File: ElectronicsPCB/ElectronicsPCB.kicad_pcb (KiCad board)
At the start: 4 copper layers, 67.8 x 80.8 mm, 44 parts

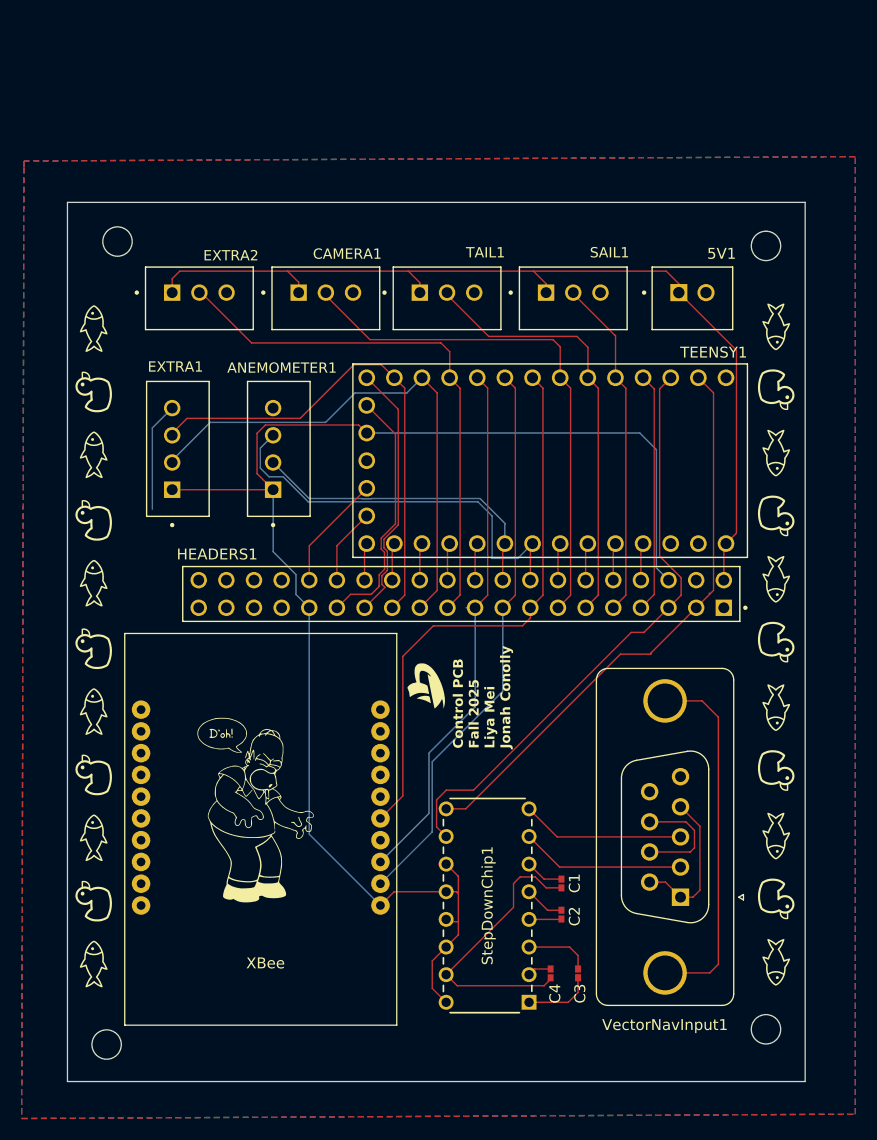
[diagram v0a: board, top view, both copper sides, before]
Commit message: overhauled controls pcb
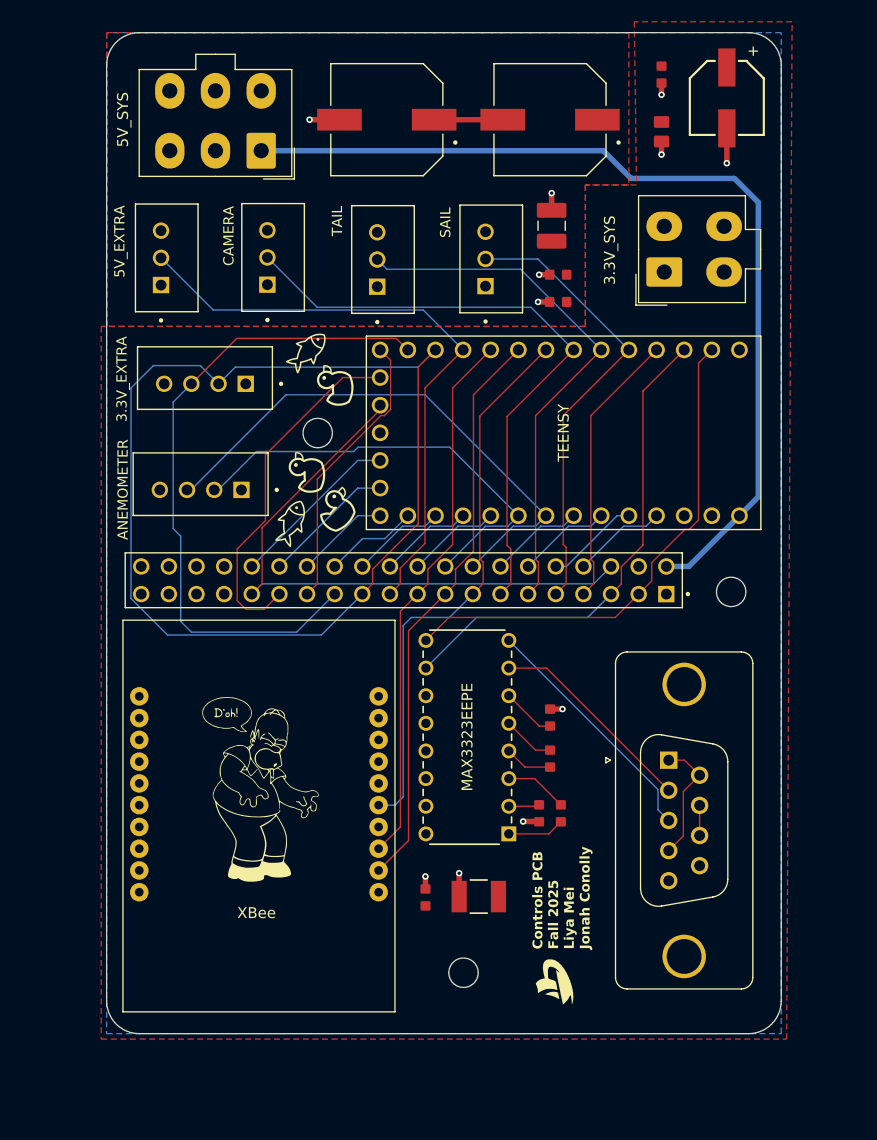
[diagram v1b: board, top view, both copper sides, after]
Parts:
- removed 5V1: B2B-XH-A, ElectronicsFootprints:B2B-XH-A
- removed the G*** at (162.5, 110.8)
- removed the G*** at (162.6, 104.8)
- removed the G*** at (162.6, 69.8)
- removed the G*** at (162.5, 87.2)
- removed the G*** at (99.8, 87.6)
- removed the G*** at (162.5, 99.0)
- removed the G*** at (162.6, 81.4)
- removed the G*** at (99.8, 122.6)
- removed the G*** at (99.8, 81.8)
- removed the G*** at (99.8, 111.0)
- removed the G*** at (99.8, 64.2)
- removed the G*** at (99.8, 99.4)
- removed the G*** at (162.5, 75.6)
- removed the G*** at (162.6, 116.6)
- removed the G*** at (99.8, 75.8)
- removed the G*** at (162.6, 93.0)
- removed the G*** at (99.8, 105.2)
- removed the G*** at (162.5, 122.4)
- removed the G*** at (99.8, 70.0)
- removed the G*** at (99.8, 93.6)
- removed the G*** at (162.5, 64.0)
- removed H4: MountingHole, MountingHole:MountingHole_2.7mm
- added 3.3V_BULK: 220uf, ElectronicsFootprints:CAP_87510_220uf, F.Cu at (158.0, 43.0)
- added 3.3V_LOW1: 0.1uf, ElectronicsFootprints:CAP_CL10B_01uf_0603, F.Cu at (152.0, 40.9)
- added 3.3V_MID1: 10uf, ElectronicsFootprints:CAP_CL21A_10uf_0805, F.Cu at (152.0, 46.1)
- added 3.3V_SYS: Conn_02x02_Counter_Clockwise, Connector_Molex:Molex_Mini-Fit_Jr_5566-04A_2x02_P4.20mm_Vertical, F.Cu at (152.2, 59.0)
- added 5V_BULK1: 1000uf, ElectronicsFootprints:CAP_EEE1A_1000uf, F.Cu at (141.8, 45.0)
- added 5V_BULK2: 1000uf, ElectronicsFootprints:CAP_EEE1A_1000uf, F.Cu at (126.8, 45.0)
- added 5V_LOW1: 0.1uf, ElectronicsFootprints:CAP_CL10B_01uf_0603, F.Cu at (142.5, 61.8)
- added 5V_MID1: 22uf, ElectronicsFootprints:CAP_CL32A_22uf_1210, F.Cu at (141.9, 54.8)
- added 5V_SYS: Conn_02x03_Counter_Clockwise, Connector_Molex:Molex_Mini-Fit_Jr_5566-06A_2x03_P4.20mm_Vertical, F.Cu at (115.2, 47.9)
- added C5: 0.1µF, ElectronicsFootprints:CAP_CL10B_01uf_0603, F.Cu at (130.3, 116.5)
- added C7: 47µF, ElectronicsFootprints:CAP_C3225_47uf_1210, F.Cu at (135.2, 116.4)
- added G***: LOGO, LOGO, F.Cu at (119.4, 77.4)
- added G***: LOGO, LOGO, F.Cu at (118.0, 82.0)
- added G***: LOGO, LOGO, F.Cu at (119.5, 66.2)
- added G***: LOGO, LOGO, F.Cu at (122.2, 80.8)
- added TeensyC0.1: 0.1µF, ElectronicsFootprints:CAP_CL10B_01uf_0603, F.Cu at (142.5, 59.2)
- C1, C2, C3, C4: footprint ElectronicsFootprints:C0402C104K4RACTU_0.1µF -> ElectronicsFootprints:CAP_CL10B_01uf_0603
- moved H1 74.3 mm to (133.8, 123.4)
- moved H3 70.9 mm to (158.4, 88.4)
- moved G*** 52.3 mm to (122.0, 69.4)
- moved H2 44.6 mm to (120.4, 73.8)
- moved G*** 29.6 mm to (142.2, 124.2)
- moved MAX3323EEPE 15.6 mm to (138.0, 110.6)
- moved C1 15.3 mm to (141.8, 100.0), turned to 90 degrees
- moved C3 14.8 mm to (142.8, 108.8)
- moved C4 14.7 mm to (140.8, 108.8)
- moved C2 14.4 mm to (141.8, 103.7)
- moved VectorNavInput1 12.6 mm to (152.7, 103.9), turned to 90 degrees
- moved SAIL 8.36 mm to (136.3, 57.8), turned to -90 degrees
- moved ANEMOMETER 7.89 mm to (109.6, 78.5), turned to 0 degrees
- moved 3.3V_EXTRA 6.97 mm to (110.0, 68.8), turned to 0 degrees
- moved TAIL 6.88 mm to (126.4, 57.9), turned to -90 degrees
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- renumbered EXTRA1 to 3.3V_EXTRA, EXTRA2 to 5V_EXTRA, ANEMOMETER1 to ANEMOMETER, CAMERA1 to CAMERA, StepDownChip1 to MAX3323EEPE, SAIL1 to SAIL, TAIL1 to TAIL, TEENSY1 to TEENSY
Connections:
- net +5V renamed +5V_SYS
- 3.3V_EXTRA pad 1: +3.3V -> +3.3V_SYS
- ANEMOMETER pad 1: +3.3V -> +3.3V_SYS
- HEADERS1 pad 31: +3.3V -> TEENSY_3.3V
- HEADERS1 pad 37: unconnected-(HEADERS1-Pad37) -> +3.3V_SYS
- HEADERS1 pad 38: unconnected-(HEADERS1-Pad38) -> +3.3V_SYS
- HEADERS1 pad 39: unconnected-(HEADERS1-Pad39) -> +3.3V_SYS
- HEADERS1 pad 40: unconnected-(HEADERS1-Pad40) -> +3.3V_SYS
- HEADERS1 pad 6: +3.3V -> TEENSY_3.3V
- MAX3323EEPE pad 11: +3.3V -> +3.3V_SYS
- MAX3323EEPE pad 12: +3.3V -> +3.3V_SYS
- MAX3323EEPE pad 13: +3.3V -> +3.3V_SYS
- MAX3323EEPE pad 14: +3.3V -> +3.3V_SYS
- MAX3323EEPE pad 16: +3.3V -> +3.3V_SYS
- TEENSY pad 3.3V_1: +3.3V -> TEENSY_3.3V
- XBEE1 pad 1: +3.3V -> +3.3V_SYS
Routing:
- net +3.3V: track 132.2 -> 0.00 mm
- net TEENSY_3.3V: track 0.00 -> 56.4 mm
- net Extra40: track 48.5 -> 99.6 mm
- net unconnected-(VectorNavInput1-PAD-Pad0): track 33.5 -> 0.00 mm
- net GND: track 37.2 -> 17.8 mm, vias 0 -> 11
- net Extra41: track 45.5 -> 60.9 mm
- net WindData0: track 29.0 -> 40.5 mm
- net WindData1: track 38.2 -> 49.5 mm
- net Sail: track 31.1 -> 42.1 mm
- net Tail: track 39.1 -> 49.5 mm
- net TeensyTX: track 55.2 -> 45.1 mm
- net VBAT: track 23.3 -> 32.7 mm
- net Camera: track 48.3 -> 57.2 mm
- net VectorNavTX: track 15.0 -> 22.6 mm
- net Net-(VectorNavInput1-Pad7): track 10.3 -> 2.77 mm
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- added copper zone on F.Cu, net +3.3V_SYS
- added copper zone on F.Cu, net +5V_SYS
- removed copper zone on F.Cu, net GND
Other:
- board size 67.8 x 80.8 mm -> 62 x 92 mm
- copper layers 4 -> 2
- board text added: "Controls PCB Fall 2025 Liya Mei Jonah Conolly"
- board text removed: "Control PCB Fall 2025 Liya Mei Jonah Conolly"

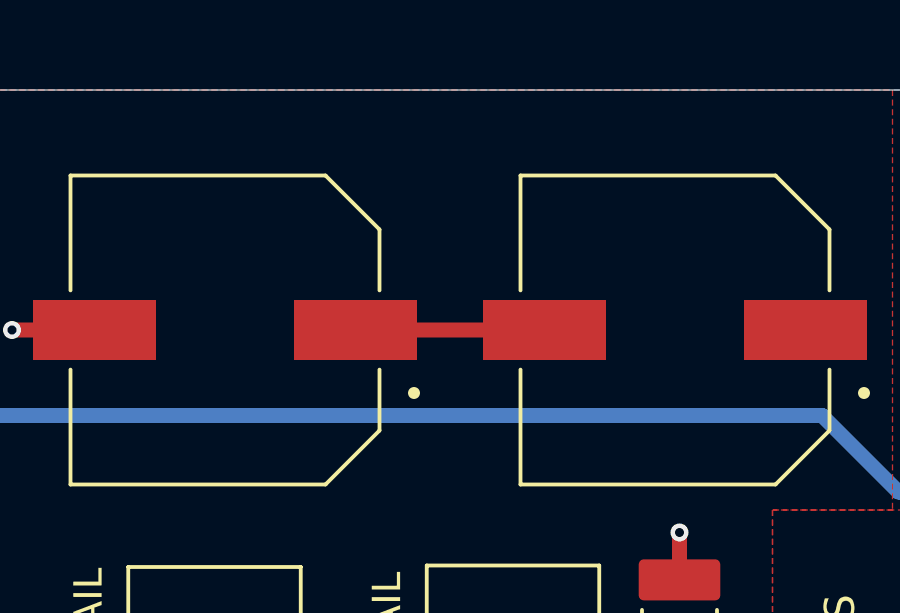
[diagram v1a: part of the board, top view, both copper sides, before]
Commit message: caps should be in parallel not series
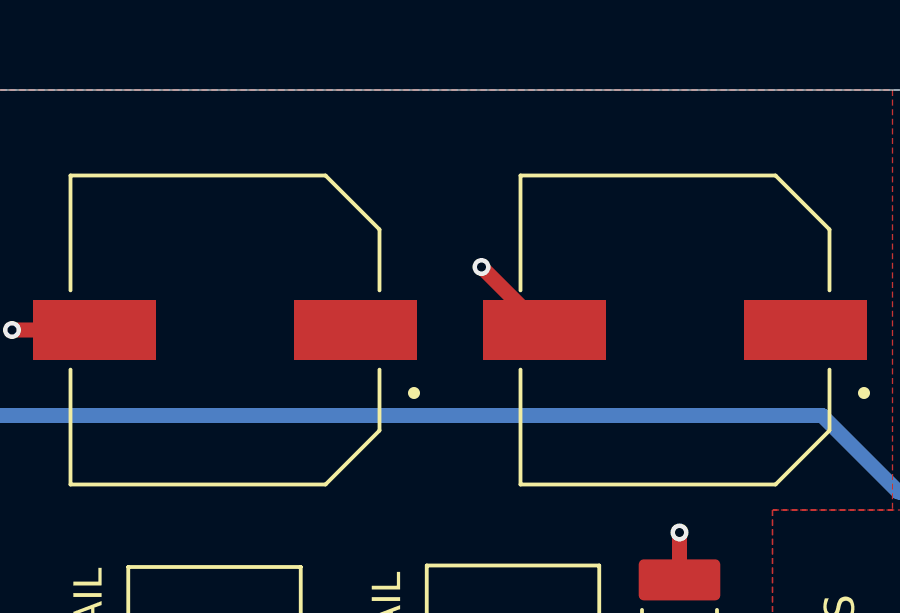
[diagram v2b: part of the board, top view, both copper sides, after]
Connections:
- 5V_BULK1 pad 2: Net-(5V_BULK1-Pad2) -> GND
- 5V_BULK2 pad 1: Net-(5V_BULK1-Pad2) -> +5V_SYS
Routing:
- net Net-(5V_BULK1-Pad2): track 6.30 -> 0.00 mm
- net GND: track 17.8 -> 20.8 mm, vias 11 -> 12

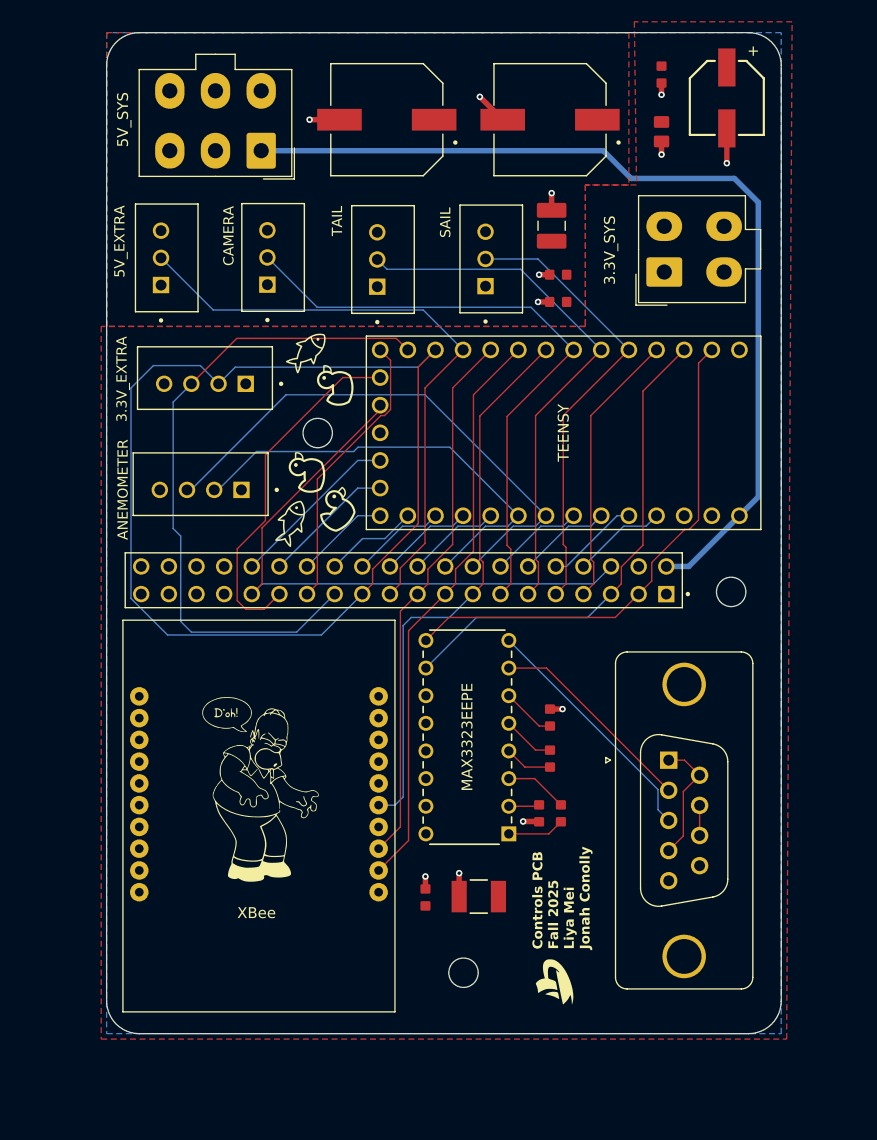
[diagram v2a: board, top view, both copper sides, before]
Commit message: moved 5v caps to more sensible spot
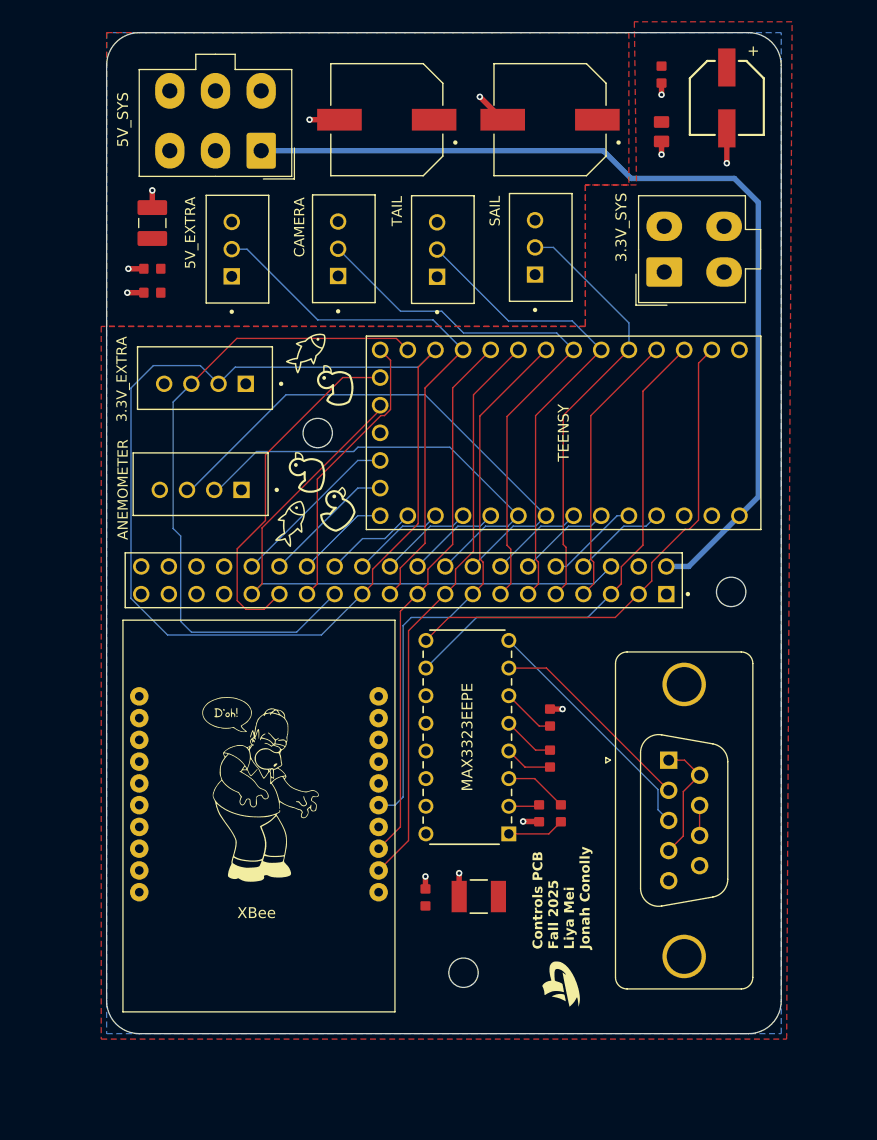
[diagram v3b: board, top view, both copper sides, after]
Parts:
- moved 5V_LOW1 37.3 mm to (105.2, 60.9)
- moved TeensyC0.1 37.3 mm to (105.2, 58.7)
- moved 5V_MID1 36.7 mm to (105.2, 54.5)
- moved 5V_EXTRA 6.55 mm to (113.0, 56.9)
- moved CAMERA 6.55 mm to (122.8, 56.9)
- moved TAIL 5.58 mm to (131.9, 56.9)
- moved SAIL 4.67 mm to (140.9, 56.7)
- moved G*** 0.63 mm to (142.8, 124.4)
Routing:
- net Camera: track 57.2 -> 51.0 mm
- net Extra3: track 56.5 -> 50.3 mm
- net Tail: track 49.5 -> 44.3 mm
- net Sail: track 42.1 -> 39.4 mm
- net GND: track 20.8 -> 21.7 mm
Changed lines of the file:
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@@
 	(footprint "ElectronicsFootprints:CAP_CL10B_01uf_0603"
 		(layer "F.Cu")
-		(at 142.5 61.75 180)
+		(at 105.2 60.9 180)
 		(property "Reference" "5V_LOW1"
 			(at -0.21 -1.05 0)
@@
 	(footprint "ElectronicsFootprints:B3B-XH-A"
 		(layer "F.Cu")
-		(at 116.3 57.6625 -90)
+		(at 122.8 56.8625 -90)
 		(property "Reference" "CAMERA"
 			(at -1.975 4.075 90)
@@
 	(footprint "ElectronicsFootprints:CAP_CL10B_01uf_0603"
 		(layer "F.Cu")
-		(at 142.5 59.25 180)
+		(at 105.2 58.7 180)
 		(property "Reference" "TeensyC0.1"
 			(at -0.21 -1.05 0)
@@
 	(footprint "ElectronicsFootprints:B3B-XH-A"
 		(layer "F.Cu")
-		(at 136.35 57.8 -90)
+		(at 140.9 56.7375 -90)
 		(property "Reference" "SAIL"
 			(at -3.3375 4.2 90)
@@
 	(footprint "ElectronicsFootprints:CAP_CL32A_22uf_1210"
 		(layer "F.Cu")
-		(at 141.9 54.75 90)
+		(at 105.2 54.5 90)
 		(property "Reference" "5V_MID1"
 			(at -1.11 -1.95 90)
@@
 	(footprint "LOGO"
 		(layer "F.Cu")
-		(at 142.2 124.2 90)
+		(at 142.8 124.4 90)
 		(property "Reference" "G***"
 			(at 0 0 90)
@@
 	(footprint "ElectronicsFootprints:B3B-XH-A"
 		(layer "F.Cu")
-		(at 126.4 57.85 -90)
+		(at 131.9 56.9375 -90)
 		(property "Reference" "TAIL"
 			(at -3.5375 4.2 90)
@@
 		(tags "connector Molex Mini-Fit_Jr vertical")
 		(property "Reference" "3.3V_SYS"
-			(at 2 -5 90)
+			(at 4.1 -3.95 90)
 			(layer "F.SilkS")
 			(effects
@@
 	(footprint "ElectronicsFootprints:B3B-XH-A"
 		(layer "F.Cu")
-		(at 106.525 57.7 -90)
+		(at 113.025 56.9 -90)
 		(property "Reference" "5V_EXTRA"
 			(at -1.5 4.325 90)
@@
 	)
 	(segment
+		(start 103 58.7)
+		(end 104.42 58.7)
+		(width 0.5)
+		(layer "F.Cu")
+		(net 1)
+	)
+	(segment
 		(start 135.3 42.9)
 		(end 137.4 45)
@@
 	)
 	(segment
-		(start 140.53 109.53)
-		(end 140.75 109.53)
+		(start 105.2 51.5)
+		(end 105.2 53.079)
 		(width 0.5)
 		(layer "F.Cu")
@@
 	)
 	(segment
-		(start 140.75 59.25)
-		(end 141.72 59.25)
+		(start 140.53 109.53)
+		(end 140.75 109.53)
 		(width 0.5)
 		(layer "F.Cu")
@@
 	)
 	(segment
-		(start 140.65 61.75)
-		(end 141.72 61.75)
+		(start 102.9 60.9)
+		(end 104.42 60.9)
 		(width 0.5)
 		(layer "F.Cu")
@@
 		(net 1)
 	)
-	(segment
-		(start 141.9 51.75)
-		(end 141.9 53.329)
-		(width 0.5)
-		(layer "F.Cu")
-		(net 1)
-	)
 	(via
 		(at 152 48.205)
@@
 	)
 	(via
-		(at 140.65 61.75)
+		(at 102.9 60.9)
 		(size 0.6)
 		(drill 0.3)
@@
 	)
 	(via
-		(at 140.75 59.25)
+		(at 103 58.7)
 		(size 0.6)
 		(drill 0.3)
@@
 	)
 	(via
-		(at 141.9 51.75)
+		(at 105.2 51.5)
 		(size 0.6)
 		(drill 0.3)
@@
 	)
 	(segment
-		(start 140.0015 62.2415)
-		(end 143.92 66.16)
+		(start 131.8 62.6)
+		(end 133.8 64.6)
+		(width 0.127)
+		(layer "B.Cu")
+		(net 11)
+	)
+	(segment
+		(start 128.0125 62.6)
+		(end 131.8 62.6)
 		(width 0.127)
 		(layer "B.Cu")
@@
 	)
 	(segment
-		(start 115.775 57.6625)
-		(end 120.354 62.2415)
+		(start 122.275 56.8625)
+		(end 128.0125 62.6)
 		(width 0.127)
 		(layer "B.Cu")
@@
 	)
 	(segment
-		(start 120.354 62.2415)
-		(end 140.0015 62.2415)
+		(start 133.8 64.6)
+		(end 142.36 64.6)
+		(width 0.127)
+		(layer "B.Cu")
+		(net 11)
+	)
+	(segment
+		(start 142.36 64.6)
+		(end 143.92 66.16)
 		(width 0.127)
 		(layer "B.Cu")
@@
 	)
 	(segment
-		(start 130.0965 62.4965)
-		(end 133.76 66.16)
+		(start 120.4 63.4)
+		(end 131 63.4)
+		(width 0.127)
+		(layer "B.Cu")
+		(net 12)
+	)
+	(segment
+		(start 112.5 56.9)
+		(end 113.9 56.9)
 		(width 0.127)
 		(layer "B.Cu")
@@
 	)
 	(segment
-		(start 106 57.7)
-		(end 110.7965 62.4965)
+		(start 113.9 56.9)
+		(end 120.4 63.4)
 		(width 0.127)
 		(layer "B.Cu")
@@
 	)
 	(segment
-		(start 110.7965 62.4965)
-		(end 130.0965 62.4965)
+		(start 131 63.4)
+		(end 133.76 66.16)
 		(width 0.127)
 		(layer "B.Cu")
@@
 	)
 	(segment
-		(start 139.0455 58.7455)
+		(start 143.8 63.5)
 		(end 146.46 66.16)
 		(width 0.127)
@@
 	)
 	(segment
-		(start 125.875 57.85)
-		(end 126.7705 58.7455)
+		(start 137.9375 63.5)
+		(end 143.8 63.5)
 		(width 0.127)
 		(layer "B.Cu")
@@
 	)
 	(segment
-		(start 126.7705 58.7455)
-		(end 139.0455 58.7455)
+		(start 131.375 56.9375)
+		(end 137.9375 63.5)
 		(width 0.127)
 		(layer "B.Cu")
@@
 	)
 	(segment
-		(start 135.825 57.8)
-		(end 140.64 57.8)
+		(start 149 63.675)
+		(end 149 66.16)
 		(width 0.127)
 		(layer "B.Cu")
@@
 	)
 	(segment
-		(start 140.64 57.8)
-		(end 149 66.16)
+		(start 142.0625 56.7375)
+		(end 149 63.675)
+		(width 0.127)
+		(layer "B.Cu")
+		(net 21)
+	)
+	(segment
+		(start 140.375 56.7375)
+		(end 142.0625 56.7375)
 		(width 0.127)
 		(layer "B.Cu")

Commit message: few other tweaks. Once I verify the stepdown stuff works, I think this is good to order
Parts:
- moved C7 5.57 mm to (129.9, 118.1), turned to 90 degrees
- moved C5 2.71 mm to (129.9, 113.8), turned to 0 degrees
- moved H1 2.16 mm to (135.9, 123.9)
- moved H2 1.36 mm to (121.5, 73.0)
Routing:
- net GND: track 21.7 -> 22.1 mm, vias 12 -> 27
